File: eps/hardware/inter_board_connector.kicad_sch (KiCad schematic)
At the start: 1 part, among them J10 Conn_02x20_Counter_Clockwise

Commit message: add stm32 bsp and reconfigure pinout
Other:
- company: (none) -> SCRT
- title: (none) -> OSUSat CubeSat EPS
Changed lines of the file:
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@@
 	(generator_version "9.0")
 	(paper "A4")
+	(title_block
+		(title "OSUSat CubeSat EPS")
+		(date "2025-08-22")
+		(rev "1")
+		(company "SCRT")
+	)
 	(rectangle
 		(start 101.6 68.072)

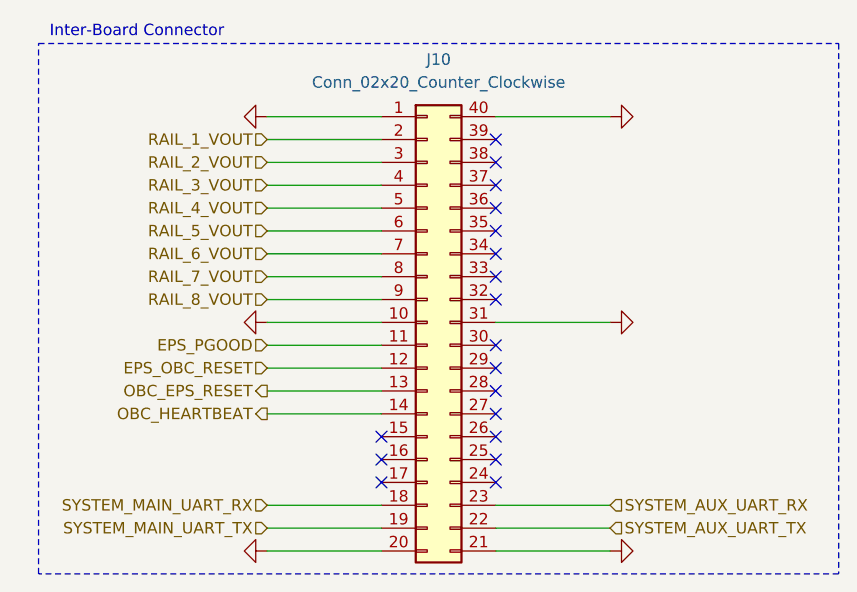
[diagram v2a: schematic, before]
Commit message: add ADC for MPPT sampling
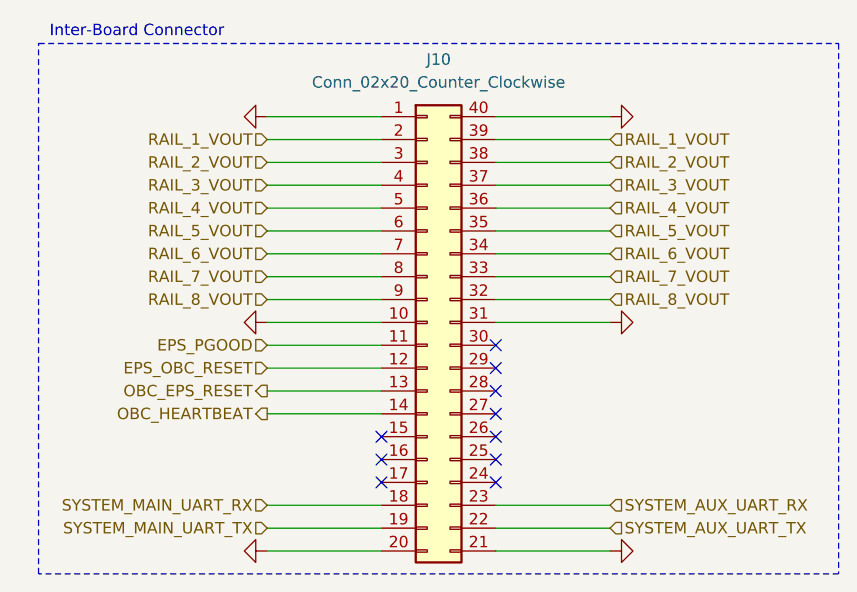
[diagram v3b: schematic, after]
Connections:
- net RAIL_1_VOUT: now also J10.39 (Pin_39)
- net RAIL_2_VOUT: now also J10.38 (Pin_38)
- net RAIL_3_VOUT: now also J10.37 (Pin_37)
- net RAIL_4_VOUT: now also J10.36 (Pin_36)
- net RAIL_5_VOUT: now also J10.35 (Pin_35)
- net RAIL_6_VOUT: now also J10.34 (Pin_34)
- net RAIL_7_VOUT: now also J10.33 (Pin_33)
- net RAIL_8_VOUT: now also J10.32 (Pin_32)
- no-connect marks 18 -> 10
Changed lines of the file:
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@@
-	)
-	(no_connect
-		(at 152.4 78.74)
 	)
 	(no_connect
@@
 	)
 	(no_connect
-		(at 152.4 83.82)
-	)
-	(no_connect
-		(at 152.4 86.36)
-	)
-	(no_connect
 		(at 139.7 114.3)
 	)
@@
 		(at 139.7 111.76)
 	)
-	(no_connect
-		(at 152.4 93.98)
-	)
-	(no_connect
-		(at 152.4 96.52)
-	)
-	(no_connect
-		(at 152.4 91.44)
-	)
-	(no_connect
-		(at 152.4 81.28)
-	)
-	(no_connect
-		(at 152.4 88.9)
+	(wire
+		(pts
+			(xy 152.4 91.44) (xy 165.1 91.44)
+		)
+		(stroke
+			(width 0)
+			(type default)
+		)
+	)
+	(wire
+		(pts
+			(xy 152.4 83.82) (xy 165.1 83.82)
+		)
+		(stroke
+			(width 0)
+			(type default)
+		)
 	)
 	(wire
@@
 	(wire
 		(pts
+			(xy 152.4 86.36) (xy 165.1 86.36)
+		)
+		(stroke
+			(width 0)
+			(type default)
+		)
+	)
+	(wire
+		(pts
+			(xy 152.4 81.28) (xy 165.1 81.28)
+		)
+		(stroke
+			(width 0)
+			(type default)
+		)
+	)
+	(wire
+		(pts
 			(xy 127 76.2) (xy 139.7 76.2)
 		)
@@
 	(wire
 		(pts
+			(xy 152.4 93.98) (xy 165.1 93.98)
+		)
+		(stroke
+			(width 0)
+			(type default)
+		)
+	)
+	(wire
+		(pts
 			(xy 127 96.52) (xy 139.7 96.52)
 		)
@@
 	(wire
 		(pts
+			(xy 152.4 96.52) (xy 165.1 96.52)
+		)
+		(stroke
+			(width 0)
+			(type default)
+		)
+	)
+	(wire
+		(pts
 			(xy 127 83.82) (xy 139.7 83.82)
 		)
@@
 	(wire
 		(pts
+			(xy 152.4 78.74) (xy 165.1 78.74)
+		)
+		(stroke
+			(width 0)
+			(type default)
+		)
+	)
+	(wire
+		(pts
 			(xy 127 91.44) (xy 139.7 91.44)
 		)
@@
 	(wire
 		(pts
+			(xy 152.4 88.9) (xy 165.1 88.9)
+		)
+		(stroke
+			(width 0)
+			(type default)
+		)
+	)
+	(wire
+		(pts
 			(xy 127 124.46) (xy 139.7 124.46)
 		)
@@
 			(width 0)
 			(type default)
+		)
+	)
+	(hierarchical_label "RAIL_6_VOUT"
+		(shape input)
+		(at 165.1 91.44 0)
+		(effects
+			(font
+				(size 1.27 1.27)
+			)
+			(justify left)
 		)
 	)
@@
 		)
 	)
+	(hierarchical_label "RAIL_2_VOUT"
+		(shape input)
+		(at 165.1 81.28 0)
+		(effects
+			(font
+				(size 1.27 1.27)
+			)
+			(justify left)
+		)
+	)
+	(hierarchical_label "RAIL_7_VOUT"
+		(shape input)
+		(at 165.1 93.98 0)
+		(effects
+			(font
+				(size 1.27 1.27)
+			)
+			(justify left)
+		)
+	)
 	(hierarchical_label "RAIL_6_VOUT"
 		(shape input)
@@
 		)
 	)
+	(hierarchical_label "RAIL_1_VOUT"
+		(shape input)
+		(at 165.1 78.74 0)
+		(effects
+			(font
+				(size 1.27 1.27)
+			)
+			(justify left)
+		)
+	)
 	(hierarchical_label "SYSTEM_AUX_UART_TX"
 		(shape input)
@@
 		)
 	)
+	(hierarchical_label "RAIL_3_VOUT"
+		(shape input)
+		(at 165.1 83.82 0)
+		(effects
+			(font
+				(size 1.27 1.27)
+			)
+			(justify left)
+		)
+	)
 	(hierarchical_label "EPS_OBC_RESET"
 		(shape input)
@@
 		)
 	)
+	(hierarchical_label "RAIL_8_VOUT"
+		(shape input)
+		(at 165.1 96.52 0)
+		(effects
+			(font
+				(size 1.27 1.27)
+			)
+			(justify left)
+		)
+	)
 	(hierarchical_label "RAIL_5_VOUT"
 		(shape input)
@@
 		)
 	)
+	(hierarchical_label "RAIL_4_VOUT"
+		(shape input)
+		(at 165.1 86.36 0)
+		(effects
+			(font
+				(size 1.27 1.27)
+			)
+			(justify left)
+		)
+	)
 	(hierarchical_label "RAIL_3_VOUT"
 		(shape input)
@@
 		)
 	)
+	(hierarchical_label "RAIL_5_VOUT"
+		(shape input)
+		(at 165.1 88.9 0)
+		(effects
+			(font
+				(size 1.27 1.27)
+			)
+			(justify left)
+		)
+	)

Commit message: finish footprint assignment and board setup
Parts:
- J10: footprint (none) -> footprints:SAMTEC_ERM8-020-X-X-DV
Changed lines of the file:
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@@
 			)
 		)
-		(property "Footprint" ""
+		(property "Footprint" "footprints:SAMTEC_ERM8-020-X-X-DV"
 			(at 144.78 99.06 0)
 			(effects

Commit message: fix update errors
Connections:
- net GND: now also J10.01 (Pin_1); no longer J10.1 (Pin_1)
- net RAIL_1_VOUT: now also J10.02 (Pin_2); no longer J10.2 (Pin_2)
- net RAIL_2_VOUT: now also J10.03 (Pin_3); no longer J10.3 (Pin_3)
- net RAIL_3_VOUT: now also J10.04 (Pin_4); no longer J10.4 (Pin_4)
- net RAIL_4_VOUT: now also J10.05 (Pin_5); no longer J10.5 (Pin_5)
- net RAIL_5_VOUT: now also J10.06 (Pin_6); no longer J10.6 (Pin_6)
- net RAIL_6_VOUT: now also J10.07 (Pin_7); no longer J10.7 (Pin_7)
- net RAIL_7_VOUT: now also J10.08 (Pin_8); no longer J10.8 (Pin_8)
- net RAIL_8_VOUT: now also J10.09 (Pin_9); no longer J10.9 (Pin_9)
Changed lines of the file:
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@@
 		(pin "31"
 		)
-		(pin "8"
+		(pin "03"
 		)
 		(pin "12"
@@
 		(pin "15"
 		)
-		(pin "7"
+		(pin "07"
 		)
 		(pin "21"
 		)
-		(pin "5"
+		(pin "08"
 		)
 		(pin "18"
@@
 		(pin "23"
 		)
-		(pin "4"
+		(pin "04"
 		)
 		(pin "25"
@@
 		(pin "30"
 		)
-		(pin "3"
+		(pin "06"
 		)
 		(pin "28"
@@
 		(pin "34"
 		)
-		(pin "2"
+		(pin "05"
 		)
-		(pin "6"
+		(pin "02"
 		)
-		(pin "1"
+		(pin "09"
 		)
 		(pin "26"
 		)
-		(pin "9"
+		(pin "01"
 		)
 		(pin "35"

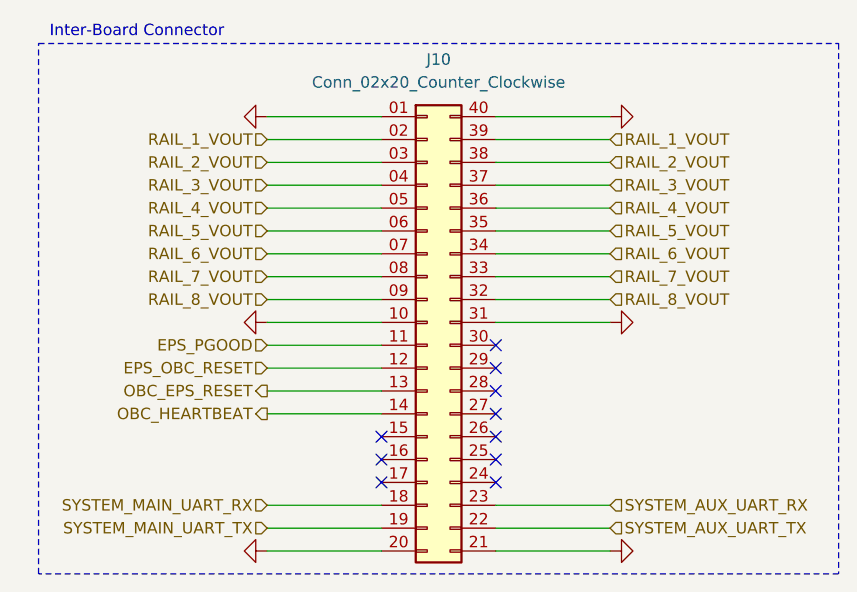
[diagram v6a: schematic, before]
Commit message: start routing i2c signals
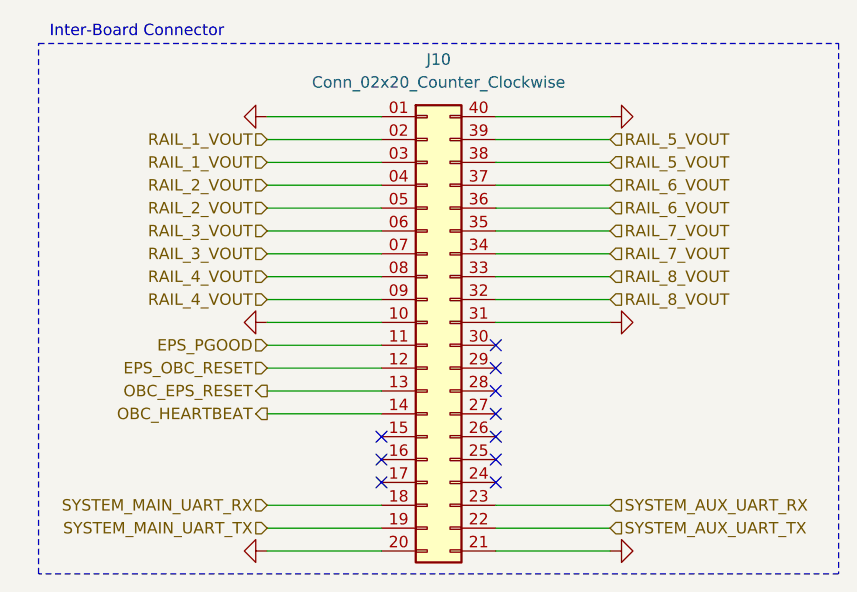
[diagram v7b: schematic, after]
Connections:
- net RAIL_1_VOUT: now also J10.03 (Pin_3); no longer J10.39 (Pin_39)
- net RAIL_2_VOUT: now also J10.04 (Pin_4), J10.05 (Pin_5); no longer J10.03 (Pin_3), J10.38 (Pin_38)
- net RAIL_3_VOUT: now also J10.06 (Pin_6), J10.07 (Pin_7); no longer J10.04 (Pin_4), J10.37 (Pin_37)
- net RAIL_4_VOUT: now also J10.08 (Pin_8), J10.09 (Pin_9); no longer J10.05 (Pin_5), J10.36 (Pin_36)
- net RAIL_5_VOUT: now also J10.38 (Pin_38), J10.39 (Pin_39); no longer J10.06 (Pin_6), J10.35 (Pin_35)
- net RAIL_6_VOUT: now also J10.36 (Pin_36), J10.37 (Pin_37); no longer J10.07 (Pin_7), J10.34 (Pin_34)
- net RAIL_7_VOUT: now also J10.34 (Pin_34), J10.35 (Pin_35); no longer J10.08 (Pin_8), J10.33 (Pin_33)
- net RAIL_8_VOUT: now also J10.33 (Pin_33); no longer J10.09 (Pin_9)
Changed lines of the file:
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@@
 		)
 	)
-	(hierarchical_label "RAIL_6_VOUT"
-		(shape input)
-		(at 165.1 91.44 0)
+	(hierarchical_label "RAIL_7_VOUT"
+		(shape input)
+		(at 165.1 88.9 0)
+		(effects
+			(font
+				(size 1.27 1.27)
+			)
+			(justify left)
+		)
+	)
+	(hierarchical_label "RAIL_1_VOUT"
+		(shape input)
+		(at 127 81.28 180)
+		(effects
+			(font
+				(size 1.27 1.27)
+			)
+			(justify right)
+		)
+	)
+	(hierarchical_label "RAIL_5_VOUT"
+		(shape input)
+		(at 165.1 81.28 0)
 		(effects
 			(font
@@
 		)
 	)
+	(hierarchical_label "RAIL_5_VOUT"
+		(shape input)
+		(at 165.1 78.74 0)
+		(effects
+			(font
+				(size 1.27 1.27)
+			)
+			(justify left)
+		)
+	)
 	(hierarchical_label "RAIL_4_VOUT"
 		(shape input)
-		(at 127 86.36 180)
-		(effects
-			(font
-				(size 1.27 1.27)
-			)
-			(justify right)
+		(at 127 96.52 180)
+		(effects
+			(font
+				(size 1.27 1.27)
+			)
+			(justify right)
+		)
+	)
+	(hierarchical_label "SYSTEM_AUX_UART_RX"
+		(shape input)
+		(at 165.1 119.38 0)
+		(effects
+			(font
+				(size 1.27 1.27)
+			)
+			(justify left)
+		)
+	)
+	(hierarchical_label "RAIL_6_VOUT"
+		(shape input)
+		(at 165.1 86.36 0)
+		(effects
+			(font
+				(size 1.27 1.27)
+			)
+			(justify left)
+		)
+	)
+	(hierarchical_label "SYSTEM_AUX_UART_TX"
+		(shape input)
+		(at 165.1 121.92 0)
+		(effects
+			(font
+				(size 1.27 1.27)
+			)
+			(justify left)
+		)
+	)
+	(hierarchical_label "EPS_OBC_RESET"
+		(shape input)
+		(at 127 104.14 180)
+		(effects
+			(font
+				(size 1.27 1.27)
+			)
+			(justify right)
+		)
+	)
+	(hierarchical_label "EPS_PGOOD"
+		(shape input)
+		(at 127 101.6 180)
+		(effects
+			(font
+				(size 1.27 1.27)
+			)
+			(justify right)
+		)
+	)
+	(hierarchical_label "RAIL_8_VOUT"
+		(shape input)
+		(at 165.1 93.98 0)
+		(effects
+			(font
+				(size 1.27 1.27)
+			)
+			(justify left)
 		)
 	)
 	(hierarchical_label "RAIL_2_VOUT"
 		(shape input)
-		(at 165.1 81.28 0)
-		(effects
-			(font
-				(size 1.27 1.27)
-			)
-			(justify left)
+		(at 127 83.82 180)
+		(effects
+			(font
+				(size 1.27 1.27)
+			)
+			(justify right)
+		)
+	)
+	(hierarchical_label "RAIL_3_VOUT"
+		(shape input)
+		(at 127 91.44 180)
+		(effects
+			(font
+				(size 1.27 1.27)
+			)
+			(justify right)
+		)
+	)
+	(hierarchical_label "RAIL_8_VOUT"
+		(shape input)
+		(at 165.1 96.52 0)
+		(effects
+			(font
+				(size 1.27 1.27)
+			)
+			(justify left)
+		)
+	)
+	(hierarchical_label "RAIL_4_VOUT"
+		(shape input)
+		(at 127 93.98 180)
+		(effects
+			(font
+				(size 1.27 1.27)
+			)
+			(justify right)
+		)
+	)
+	(hierarchical_label "SYSTEM_MAIN_UART_TX"
+		(shape input)
+		(at 127 121.92 180)
+		(effects
+			(font
+				(size 1.27 1.27)
+			)
+			(justify right)
+		)
+	)
+	(hierarchical_label "RAIL_1_VOUT"
+		(shape input)
+		(at 127 78.74 180)
+		(effects
+			(font
+				(size 1.27 1.27)
+			)
+			(justify right)
+		)
+	)
+	(hierarchical_label "RAIL_6_VOUT"
+		(shape input)
+		(at 165.1 83.82 0)
+		(effects
+			(font
+				(size 1.27 1.27)
+			)
+			(justify left)
+		)
+	)
+	(hierarchical_label "RAIL_3_VOUT"
+		(shape input)
+		(at 127 88.9 180)
+		(effects
+			(font
+				(size 1.27 1.27)
+			)
+			(justify right)
 		)
 	)
 	(hierarchical_label "RAIL_7_VOUT"
 		(shape input)
-		(at 165.1 93.98 0)
-		(effects
-			(font
-				(size 1.27 1.27)
-			)
-			(justify left)
-		)
-	)
-	(hierarchical_label "RAIL_6_VOUT"
-		(shape input)
-		(at 127 91.44 180)
-		(effects
-			(font
-				(size 1.27 1.27)
-			)
-			(justify right)
-		)
-	)
-	(hierarchical_label "SYSTEM_AUX_UART_RX"
-		(shape input)
-		(at 165.1 119.38 0)
-		(effects
-			(font
-				(size 1.27 1.27)
-			)
-			(justify left)
-		)
-	)
-	(hierarchical_label "RAIL_7_VOUT"
-		(shape input)
-		(at 127 93.98 180)
-		(effects
-			(font
-				(size 1.27 1.27)
-			)
-			(justify right)
-		)
-	)
-	(hierarchical_label "RAIL_1_VOUT"
-		(shape input)
-		(at 165.1 78.74 0)
-		(effects
-			(font
-				(size 1.27 1.27)
-			)
-			(justify left)
-		)
-	)
-	(hierarchical_label "SYSTEM_AUX_UART_TX"
-		(shape input)
-		(at 165.1 121.92 0)
-		(effects
-			(font
-				(size 1.27 1.27)
-			)
-			(justify left)
-		)
-	)
-	(hierarchical_label "RAIL_3_VOUT"
-		(shape input)
-		(at 165.1 83.82 0)
-		(effects
-			(font
-				(size 1.27 1.27)
-			)
-			(justify left)
-		)
-	)
-	(hierarchical_label "EPS_OBC_RESET"
-		(shape input)
-		(at 127 104.14 180)
-		(effects
-			(font
-				(size 1.27 1.27)
-			)
-			(justify right)
-		)
-	)
-	(hierarchical_label "EPS_PGOOD"
-		(shape input)
-		(at 127 101.6 180)
-		(effects
-			(font
-				(size 1.27 1.27)
-			)
-			(justify right)
-		)
-	)
-	(hierarchical_label "RAIL_2_VOUT"
-		(shape input)
-		(at 127 81.28 180)
-		(effects
-			(font
-				(size 1.27 1.27)
-			)
-			(justify right)
-		)
-	)
-	(hierarchical_label "RAIL_8_VOUT"
-		(shape input)
-		(at 165.1 96.52 0)
-		(effects
-			(font
-				(size 1.27 1.27)
-			)
-			(justify left)
-		)
-	)
-	(hierarchical_label "RAIL_5_VOUT"
-		(shape input)
-		(at 127 88.9 180)
-		(effects
-			(font
-				(size 1.27 1.27)
-			)
-			(justify right)
-		)
-	)
-	(hierarchical_label "RAIL_8_VOUT"
-		(shape input)
-		(at 127 96.52 180)
-		(effects
-			(font
-				(size 1.27 1.27)
-			)
-			(justify right)
-		)
-	)
-	(hierarchical_label "SYSTEM_MAIN_UART_TX"
-		(shape input)
-		(at 127 121.92 180)
-		(effects
-			(font
-				(size 1.27 1.27)
-			)
-			(justify right)
-		)
-	)
-	(hierarchical_label "RAIL_1_VOUT"
-		(shape input)
-		(at 127 78.74 180)
-		(effects
-			(font
-				(size 1.27 1.27)
-			)
-			(justify right)
-		)
-	)
-	(hierarchical_label "RAIL_4_VOUT"
-		(shape input)
-		(at 165.1 86.36 0)
-		(effects
-			(font
-				(size 1.27 1.27)
-			)
-			(justify left)
-		)
-	)
-	(hierarchical_label "RAIL_3_VOUT"
-		(shape input)
-		(at 127 83.82 180)
-		(effects
-			(font
-				(size 1.27 1.27)
-			)
-			(justify right)
-		)
-	)
-	(hierarchical_label "RAIL_5_VOUT"
-		(shape input)
-		(at 165.1 88.9 0)
+		(at 165.1 91.44 0)
 		(effects
 			(font
@@
 		(effects
 			(font
+				(size 1.27 1.27)
+			)
+			(justify right)
+		)
+	)
+	(hierarchical_label "RAIL_2_VOUT"
+		(shape input)
+		(at 127 86.36 180)
+		(effects
+			(font

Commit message: add BOM and fix tons of hardware bugs
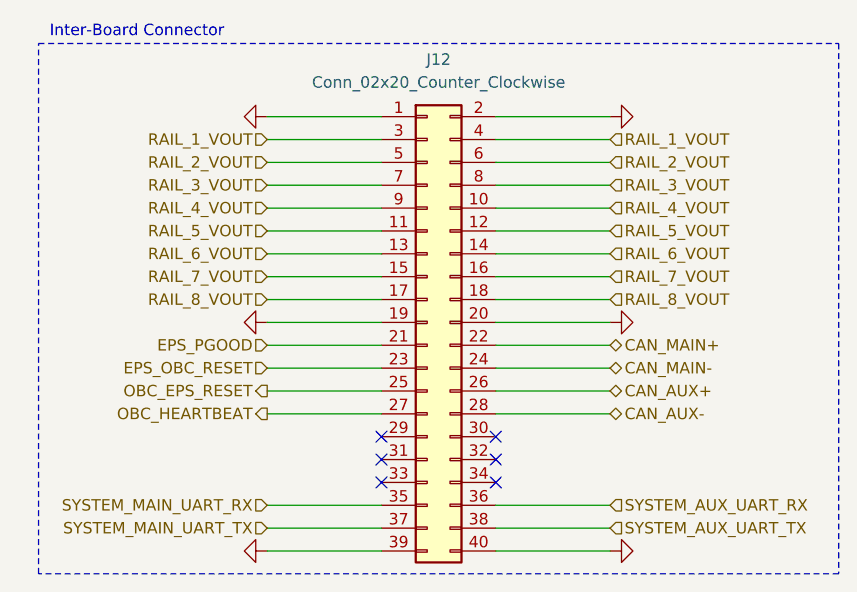
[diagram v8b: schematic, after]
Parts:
- J12: renamed from J10; footprint footprints:SAMTEC_ERM8-020-X-X-DV -> Connector_Samtec_EdgeRate:Samtec_ERM8-020-XX.X-DV_2x20_P0.8mm_Terminal; symbol Connector_Generic:Conn_02x20_Counter_Clockwise -> Connector_Generic:Conn_02x20_Odd_Even; LCSC PN (none) -> C6244310
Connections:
- net EPS_OBC_RESET: now also J12.23 (Pin_23); no longer J12.12 (Pin_12)
- net EPS_PGOOD: now also J12.21 (Pin_21); no longer J12.11 (Pin_11)
- net GND: now also J12.1 (Pin_1), J12.19 (Pin_19), J12.2 (Pin_2), J12.39 (Pin_39); no longer J12.01 (Pin_1), J12.10 (Pin_10), J12.21 (Pin_21), J12.31 (Pin_31)
- net OBC_EPS_RESET: now also J12.25 (Pin_25); no longer J12.13 (Pin_13)
- net OBC_HEARTBEAT: now also J12.27 (Pin_27); no longer J12.14 (Pin_14)
- net RAIL_1_VOUT: now also J12.3 (Pin_3), J12.4 (Pin_4); no longer J12.02 (Pin_2), J12.03 (Pin_3)
- net RAIL_2_VOUT: now also J12.5 (Pin_5), J12.6 (Pin_6); no longer J12.04 (Pin_4), J12.05 (Pin_5)
- net RAIL_3_VOUT: now also J12.7 (Pin_7), J12.8 (Pin_8); no longer J12.06 (Pin_6), J12.07 (Pin_7)
- net RAIL_4_VOUT: now also J12.10 (Pin_10), J12.9 (Pin_9); no longer J12.08 (Pin_8), J12.09 (Pin_9)
- net RAIL_5_VOUT: now also J12.11 (Pin_11), J12.12 (Pin_12); no longer J12.38 (Pin_38), J12.39 (Pin_39)
- net RAIL_6_VOUT: now also J12.13 (Pin_13), J12.14 (Pin_14); no longer J12.36 (Pin_36), J12.37 (Pin_37)
- net RAIL_7_VOUT: now also J12.15 (Pin_15), J12.16 (Pin_16); no longer J12.34 (Pin_34), J12.35 (Pin_35)
- net RAIL_8_VOUT: now also J12.17 (Pin_17), J12.18 (Pin_18); no longer J12.32 (Pin_32), J12.33 (Pin_33)
- net SYSTEM_AUX_UART_RX: now also J12.36 (Pin_36); no longer J12.23 (Pin_23)
- net SYSTEM_AUX_UART_TX: now also J12.38 (Pin_38); no longer J12.22 (Pin_22)
- net SYSTEM_MAIN_UART_RX: now also J12.35 (Pin_35); no longer J12.18 (Pin_18)
- net SYSTEM_MAIN_UART_TX: now also J12.37 (Pin_37); no longer J12.19 (Pin_19)
- net CAN_MAIN-: now reaches J12.24 (Pin_24)
- net CAN_AUX+: now reaches J12.26 (Pin_26)
- net CAN_AUX-: now reaches J12.28 (Pin_28)
- new net CAN_MAIN+: J12.22 (Pin_22)
- no-connect marks 10 -> 6
